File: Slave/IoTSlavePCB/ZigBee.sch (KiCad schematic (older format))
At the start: 0 parts

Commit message: Continued work on slaves. Added sensor and begun work on ZigBee transceiver.
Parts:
- added C? (x3): 100 nF, symbol Device:C
- added C? (x2): 22 pF, symbol Device:C
- added U?: AT86RF232-ZX, Personal_ICs:AT86RF232-ZX, symbol Personal_ICs:AT86RF232-ZX
- added X?: 16 MHz, Personal_Actives:ECS1601633BCKMTR, symbol Device:Crystal_GND24
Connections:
- new net +1V8: C?.1, C?.1, C?.2, U?.13 (DVDD), U?.14 (DVDD), U?.29 (AVDD)
- new net GND: C?.1, C?.1, C?.2, C?.2, C?.2, U?.1 (AVSS), U?.12 (DVSS), U?.16 (DVSS), U?.18 (DVSS), U?.2 (AVSS), U?.21 (DVSS), U?.27 (AVSS), U?.3 (AVSS), U?.30 (AVSS), U?.31 (AVSS), U?.32 (AVSS), U?.33 (EPAD), U?.6 (AVSS), U?.7 (DVSS), X?.2, X?.4
- new net IRQ: U?.24 (IRQ)
- new net SLP_TR: U?.11 (SLP_TR)
- new net SPI_CLK: U?.19 (SCLK)
- new net SPI_MISO: U?.20 (MISO)
- new net SPI_MOSI: U?.22 (MOSI)
- new net XI: C?.1, U?.25 (XTAL2), X?.1
- new net XO: C?.2, U?.26 (XTAL1), X?.3
- new net ~RST: U?.8 (/RST)
- new net ~SPI_SS: U?.23 (/SEL)
- no-connect marks 0 -> 3
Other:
- note added: "16 MHz Crystal"
- note added: "16 pF load capacitance.\nParasitic pin capacitance is 3 pF.\nStray board capacitance is 2 pF."
- note added: "Digital and analog ground must be separated (A/D VSS).\nAntenna impedance is 50 Ohm."
- note added: "ZigBee Transceiver"

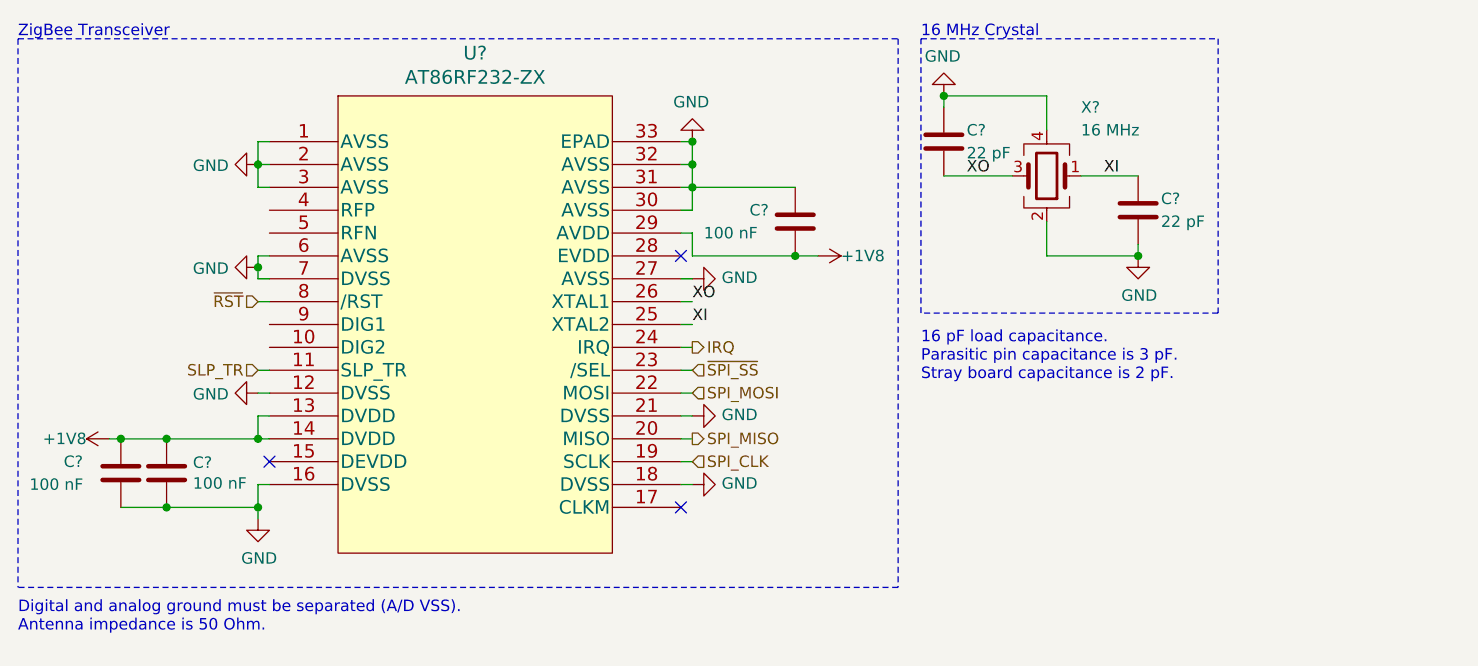
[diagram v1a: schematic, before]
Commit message: Finished slave schematics, including memory and Zigbee Transceiver. Further work on PCB, well underway.
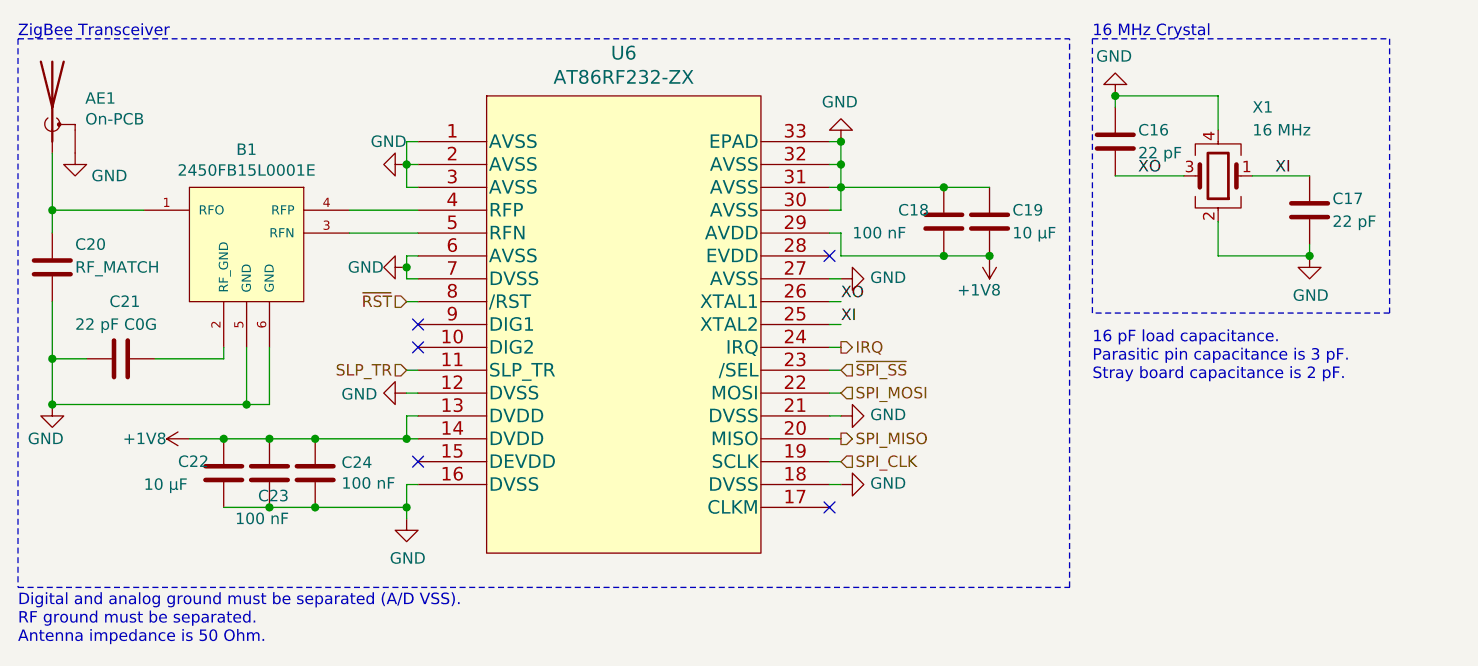
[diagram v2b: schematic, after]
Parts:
- added AE1: On-PCB, RF_Antenna:Texas_SWRA117D_2.4GHz_Right, symbol Device:Antenna_Shield
- added B1: 2450FB15L0001E, Personal_Passives:2450FB15L0001E, symbol Personal_Passives:2450FB15L0001E
- added C19, C22: 10 µF, Capacitor_SMD:C_0805_2012Metric, symbol Device:C
- added C20: RF_MATCH, Capacitor_SMD:C_0805_2012Metric, symbol Device:C
- added C21: 22 pF C0G, Capacitor_SMD:C_0402_1005Metric, symbol Device:C
- C16, C17, C18, C23, C24: renamed from C?; footprint (none) -> Capacitor_SMD:C_0603_1608Metric
- gave numbers to parts that had none: 2
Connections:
- net +1V8: now also C19.2, C22.1
- net GND: now also AE1.2 (Shield), B1.5 (GND), B1.6 (GND), C19.1, C20.2, C21.2, C22.2
- net at U6.4 (RFP): now also B1.4 (RFP)
- net at U6.5 (RFN): now also B1.3 (RFN)
- new net: AE1.1 (A), B1.1 (RFO), C20.1
- new net: B1.2 (RF_GND), C21.1
- no-connect marks 3 -> 5
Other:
- note added: "Digital and analog ground must be separated (A/D VSS).\nRF ground must be separated.\nAntenna impedance is 50 Ohm."
- note removed: "Digital and analog ground must be separated (A/D VSS).\nAntenna impedance is 50 Ohm."
- moved on the sheet: C16, C17, C18, C23, C24, U6, X1

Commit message: Made more connections on PCB, some optimizations. Added silk screen text.
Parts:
- AE1: footprint RF_Antenna:Texas_SWRA117D_2.4GHz_Right -> RF_Antenna:Texas_SWRA117D_2.4GHz_Left
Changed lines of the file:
@@
 F 0 "AE1" H 1394 1339 50  0000 L CNN
 F 1 "On-PCB" H 1394 1248 50  0000 L CNN
-F 2 "RF_Antenna:Texas_SWRA117D_2.4GHz_Right" H 1250 1400 50  0001 C CNN
+F 2 "RF_Antenna:Texas_SWRA117D_2.4GHz_Left" H 1250 1400 50  0001 C CNN
 F 3 "~" H 1250 1400 50  0001 C CNN
 	1    1250 1300

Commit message: Everything placed. Only needs final routes and optimization.
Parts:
- removed C23: 100 nF, Capacitor_SMD:C_0603_1608Metric, symbol Device:C
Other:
- moved on the sheet: C22
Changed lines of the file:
@@
 	4700 1550 4700 1650
-$Comp
-L Device:C C23
-U 1 1 5FA87196
-P 2200 2900
-F 0 "C23" H 2150 2800 50  0000 L CNN
-F 1 "100 nF" H 2050 2700 50  0000 L CNN
-F 2 "Capacitor_SMD:C_0603_1608Metric" H 2238 2750 50  0001 C CNN
-F 3 "~" H 2200 2900 50  0001 C CNN
-	1    2200 2900
-	1    0    0    -1
-$EndComp
 $Comp
 L Device:C C18
@@
 	4700 1750 4700 1650
 Wire Wire Line
-	2200 2750 2400 2750
-Connection ~ 2200 2750
-Wire Wire Line
 	2850 2650 2800 2650
 Wire Wire Line
@@
 Connection ~ 2400 2750
 Connection ~ 2400 3050
-Wire Wire Line
-	2400 3050 2200 3050
 Wire Wire Line
 	2800 2950 2800 3050
@@
 L Device:C C22
 U 1 1 5FB79D41
-P 2000 2900
-F 0 "C22" H 1800 2950 50  0000 L CNN
-F 1 "10 µF" H 1650 2850 50  0000 L CNN
-F 2 "Capacitor_SMD:C_0805_2012Metric" H 2038 2750 50  0001 C CNN
-F 3 "~" H 2000 2900 50  0001 C CNN
-	1    2000 2900
-	1    0    0    -1
-$EndComp
-Wire Wire Line
-	2000 2750 2200 2750
-Wire Wire Line
-	2000 3050 2200 3050
-Connection ~ 2200 3050
-Wire Wire Line
-	1850 2750 2000 2750
-Connection ~ 2000 2750
+P 2200 2900
+F 0 "C22" H 1950 2950 50  0000 L CNN
+F 1 "10 µF" H 1850 2850 50  0000 L CNN
+F 2 "Capacitor_SMD:C_0805_2012Metric" H 2238 2750 50  0001 C CNN
+F 3 "~" H 2200 2900 50  0001 C CNN
+	1    2200 2900
+	1    0    0    -1
+$EndComp
 Wire Notes Line
 	5700 3400 5700 1000
@@
 Wire Notes Line
 	1100 1000 5700 1000
+Connection ~ 2200 2750
+Wire Wire Line
+	2200 2750 2400 2750
+Wire Wire Line
+	2200 3050 2400 3050
+Wire Wire Line
+	1850 2750 2200 2750
 $EndSCHEMATC
